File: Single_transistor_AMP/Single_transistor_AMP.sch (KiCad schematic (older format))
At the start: 9 parts, among them J1 Signal_IN, J2 Signal_OUT, Q1 BC337

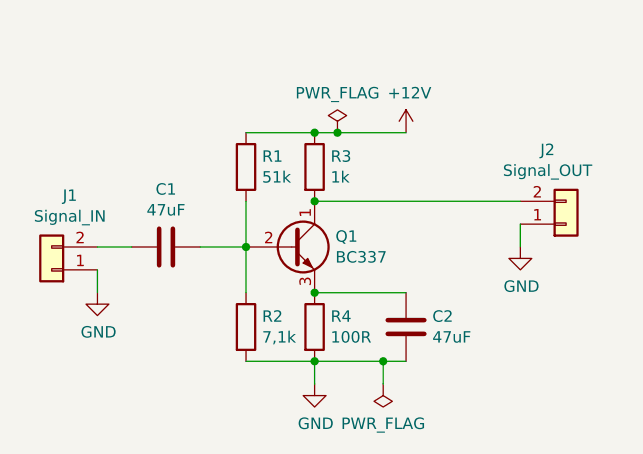
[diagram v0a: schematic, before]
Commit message: Labojums: Pievienots savienotājs +12V barošanai
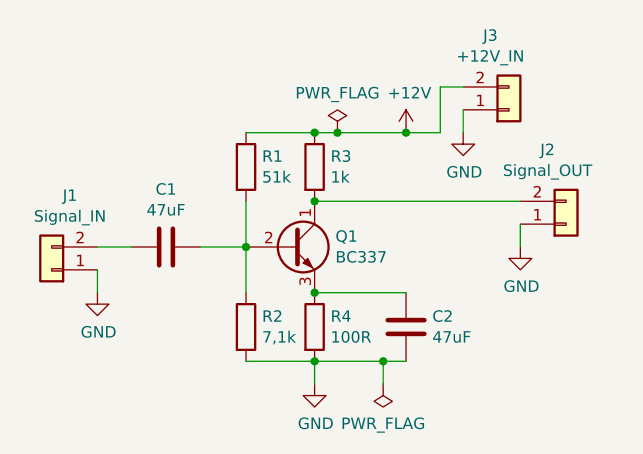
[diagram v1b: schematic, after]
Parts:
- added J3: +12V_IN, symbol Connector_Generic:Conn_01x02
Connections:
- net +12V: now also J3.2 (Pin_2)
- net GND: now also J3.1 (Pin_1)
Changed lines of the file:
@@
 Wire Wire Line
 	5950 4550 6050 4550
+$Comp
+L Connector_Generic:Conn_01x02 J3
+U 1 1 5C9CA615
+P 6500 3450
+F 0 "J3" H 6419 3125 50  0000 C CNN
+F 1 "+12V_IN" H 6419 3216 50  0000 C CNN
+F 2 "" H 6500 3450 50  0001 C CNN
+F 3 "~" H 6500 3450 50  0001 C CNN
+	1    6500 3450
+	1    0    0    1
+$EndComp
+Wire Wire Line
+	6050 3550 6200 3550
+Wire Wire Line
+	6200 3550 6200 3350
+Wire Wire Line
+	6200 3350 6300 3350
+Connection ~ 6050 3550
+Wire Wire Line
+	6300 3450 6300 3550
+$Comp
+L power:GND #PWR05
+U 1 1 5C9CB3FB
+P 6300 3550
+F 0 "#PWR05" H 6300 3300 50  0001 C CNN
+F 1 "GND" H 6305 3377 50  0000 C CNN
+F 2 "" H 6300 3550 50  0001 C CNN
+F 3 "" H 6300 3550 50  0001 C CNN
+	1    6300 3550
+	1    0    0    -1
+$EndComp
 $EndSCHEMATC

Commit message: Izlabots Single_transistor_AMP proj. (datulapas, footprints)
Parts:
- C1, C2: footprint (none) -> Single_transistor_AMP:CAPPRD250W55D630H600
- J1, J2, J3: footprint (none) -> Single_transistor_AMP:SHDR2W90P0X508_1X2_1016X950X1500P_Conn
- Q1: footprint Package_TO_SOT_THT:TO-92_Inline -> Single_transistor_AMP:Pkg_TO_SOT_THT-TO-92_Inline
- R1, R4: footprint (none) -> Single_transistor_AMP:R_2512_6332Metric
- R2: footprint (none) -> Single_transistor_AMP:R_2010_5025Metric
- R3: footprint (none) -> Single_transistor_AMP:R_1218_3246Metric
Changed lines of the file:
@@
 EESchema Schematic File Version 4
 LIBS:Single_transistor_AMP-cache
-EELAYER 29 0
+EELAYER 26 0
 EELAYER END
 $Descr A4 11693 8268
@@
 F 0 "Q1" H 5741 4096 50  0000 L CNN
 F 1 "BC337" H 5741 4005 50  0000 L CNN
-F 2 "Package_TO_SOT_THT:TO-92_Inline" H 5750 3975 50  0001 L CIN
+F 2 "Single_transistor_AMP:Pkg_TO_SOT_THT-TO-92_Inline" H 5750 3975 50  0001 L CIN
 F 3 "https://www.mouser.com/ds/2/302/BC817_BC817W_BC337-188983.pdf" H 5550 4050 50  0001 L CNN
 	1    5550 4050
@@
 F 0 "R2" H 5420 4446 50  0000 L CNN
 F 1 "7,1k" H 5420 4355 50  0000 L CNN
-F 2 "" V 5280 4400 50  0001 C CNN
-F 3 "~" H 5350 4400 50  0001 C CNN
+F 2 "Single_transistor_AMP:R_2010_5025Metric" V 5280 4400 50  0001 C CNN
+F 3 "https://eu.mouser.com/datasheet/2/447/PYu-RC_Group_51_RoHS_L_10-1527934.pdf" H 5350 4400 50  0001 C CNN
 	1    5350 4400
 	1    0    0    -1
@@
 F 0 "R3" H 5720 3746 50  0000 L CNN
 F 1 "1k" H 5720 3655 50  0000 L CNN
-F 2 "" V 5580 3700 50  0001 C CNN
-F 3 "~" H 5650 3700 50  0001 C CNN
+F 2 "Single_transistor_AMP:R_1218_3246Metric" V 5580 3700 50  0001 C CNN
+F 3 "https://eu.mouser.com/datasheet/2/447/yageodocoutput-1290830.pdf" H 5650 3700 50  0001 C CNN
 	1    5650 3700
 	1    0    0    -1
@@
 F 0 "R4" H 5720 4446 50  0000 L CNN
 F 1 "100R" H 5720 4355 50  0000 L CNN
-F 2 "" V 5580 4400 50  0001 C CNN
-F 3 "~" H 5650 4400 50  0001 C CNN
+F 2 "Single_transistor_AMP:R_2512_6332Metric" V 5580 4400 50  0001 C CNN
+F 3 "https://eu.mouser.com/datasheet/2/447/PYu-AC_51_RoHS_L_6-1152827.pdf" H 5650 4400 50  0001 C CNN
 	1    5650 4400
 	1    0    0    -1
@@
 F 0 "C1" V 4748 4050 50  0000 C CNN
 F 1 "47uF" V 4839 4050 50  0000 C CNN
-F 2 "" H 5038 3900 50  0001 C CNN
-F 3 "~" H 5000 4050 50  0001 C CNN
+F 2 "Single_transistor_AMP:CAPPRD250W55D630H600" H 5038 3900 50  0001 C CNN
+F 3 "https://eu.mouser.com/datasheet/2/315/AAB8000C265-1267026.pdf" H 5000 4050 50  0001 C CNN
 	1    5000 4050
 	0    1    1    0
@@
 F 0 "C2" H 5935 4354 50  0000 R CNN
 F 1 "47uF" H 5935 4445 50  0000 R CNN
-F 2 "" H 6088 4250 50  0001 C CNN
-F 3 "~" H 6050 4400 50  0001 C CNN
+F 2 "Single_transistor_AMP:CAPPRD250W55D630H600" H 6088 4250 50  0001 C CNN
+F 3 "https://eu.mouser.com/datasheet/2/315/AAB8000C265-1267026.pdf" H 6050 4400 50  0001 C CNN
 	1    6050 4400
 	-1   0    0    1
@@
 F 0 "J1" H 4420 3825 50  0000 C CNN
 F 1 "Signal_IN" H 4420 3916 50  0000 C CNN
-F 2 "" H 4500 4150 50  0001 C CNN
-F 3 "~" H 4500 4150 50  0001 C CNN
+F 2 "Single_transistor_AMP:SHDR2W90P0X508_1X2_1016X950X1500P_Conn" H 4500 4150 50  0001 C CNN
+F 3 "https://eu.mouser.com/datasheet/2/324/ItemDetail_1888687-919494.pdf" H 4500 4150 50  0001 C CNN
 	1    4500 4150
 	-1   0    0    1
@@
 F 0 "J2" H 6669 3625 50  0000 C CNN
 F 1 "Signal_OUT" H 6669 3716 50  0000 C CNN
-F 2 "" H 6750 3950 50  0001 C CNN
-F 3 "~" H 6750 3950 50  0001 C CNN
+F 2 "Single_transistor_AMP:SHDR2W90P0X508_1X2_1016X950X1500P_Conn" H 6750 3950 50  0001 C CNN
+F 3 "https://eu.mouser.com/datasheet/2/324/ItemDetail_1888687-919494.pdf" H 6750 3950 50  0001 C CNN
 	1    6750 3950
 	1    0    0    1
@@
 F 0 "R1" H 5420 3746 50  0000 L CNN
 F 1 "51k" H 5420 3655 50  0000 L CNN
-F 2 "" V 5280 3700 50  0001 C CNN
-F 3 "~" H 5350 3700 50  0001 C CNN
+F 2 "Single_transistor_AMP:R_2512_6332Metric" V 5280 3700 50  0001 C CNN
+F 3 "https://eu.mouser.com/datasheet/2/447/PYu-AC_51_RoHS_L_6-1152827.pdf" H 5350 3700 50  0001 C CNN
 	1    5350 3700
 	1    0    0    -1
@@
 F 0 "J3" H 6419 3125 50  0000 C CNN
 F 1 "+12V_IN" H 6419 3216 50  0000 C CNN
-F 2 "" H 6500 3450 50  0001 C CNN
-F 3 "~" H 6500 3450 50  0001 C CNN
+F 2 "Single_transistor_AMP:SHDR2W90P0X508_1X2_1016X950X1500P_Conn" H 6500 3450 50  0001 C CNN
+F 3 "https://eu.mouser.com/datasheet/2/324/ItemDetail_1888687-919494.pdf" H 6500 3450 50  0001 C CNN
 	1    6500 3450
 	1    0    0    1

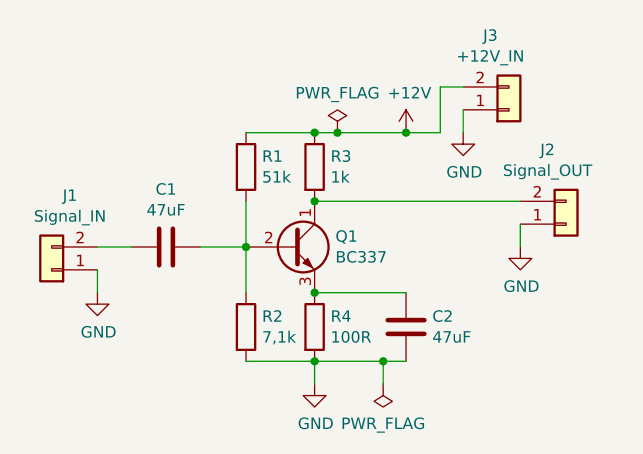
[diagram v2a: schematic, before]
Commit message: Papildināts Single_transistor_AMP projekts, pēc 8.lekcijas m.d. nosacījumiem (darbs ar Pcbnew)
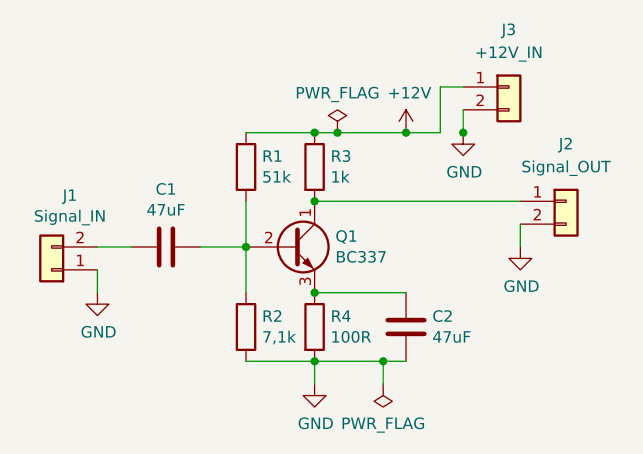
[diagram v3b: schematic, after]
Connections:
- net +12V: now also J3.1 (Pin_1); no longer J3.2 (Pin_2)
- net GND: now also J2.2 (Pin_2), J3.2 (Pin_2); no longer J2.1 (Pin_1), J3.1 (Pin_1)
- net at Q1.1 (C), R3.2: now also J2.1 (Pin_1); no longer J2.2 (Pin_2)
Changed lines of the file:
@@
 EESchema Schematic File Version 4
 LIBS:Single_transistor_AMP-cache
-EELAYER 26 0
+EELAYER 29 0
 EELAYER END
 $Descr A4 11693 8268
@@
 L Connector_Generic:Conn_01x02 J2
 U 1 1 5C8A2EFA
-P 6750 3950
-F 0 "J2" H 6669 3625 50  0000 C CNN
-F 1 "Signal_OUT" H 6669 3716 50  0000 C CNN
-F 2 "Single_transistor_AMP:SHDR2W90P0X508_1X2_1016X950X1500P_Conn" H 6750 3950 50  0001 C CNN
-F 3 "https://eu.mouser.com/datasheet/2/324/ItemDetail_1888687-919494.pdf" H 6750 3950 50  0001 C CNN
-	1    6750 3950
-	1    0    0    1
+P 6750 3850
+F 0 "J2" H 6750 4100 50  0000 C CNN
+F 1 "Signal_OUT" H 6750 4000 50  0000 C CNN
+F 2 "Single_transistor_AMP:SHDR2W90P0X508_1X2_1016X950X1500P_Conn" H 6750 3850 50  0001 C CNN
+F 3 "https://eu.mouser.com/datasheet/2/324/ItemDetail_1888687-919494.pdf" H 6750 3850 50  0001 C CNN
+	1    6750 3850
+	1    0    0    -1
 $EndComp
 $Comp
@@
 Wire Wire Line
 	5650 3850 6550 3850
-Wire Wire Line
-	6550 3950 6550 4050
 Connection ~ 5650 3550
 Wire Wire Line
@@
 L Connector_Generic:Conn_01x02 J3
 U 1 1 5C9CA615
-P 6500 3450
-F 0 "J3" H 6419 3125 50  0000 C CNN
-F 1 "+12V_IN" H 6419 3216 50  0000 C CNN
-F 2 "Single_transistor_AMP:SHDR2W90P0X508_1X2_1016X950X1500P_Conn" H 6500 3450 50  0001 C CNN
-F 3 "https://eu.mouser.com/datasheet/2/324/ItemDetail_1888687-919494.pdf" H 6500 3450 50  0001 C CNN
-	1    6500 3450
-	1    0    0    1
+P 6500 3350
+F 0 "J3" H 6500 3600 50  0000 C CNN
+F 1 "+12V_IN" H 6500 3500 50  0000 C CNN
+F 2 "Single_transistor_AMP:SHDR2W90P0X508_1X2_1016X950X1500P_Conn" H 6500 3350 50  0001 C CNN
+F 3 "https://eu.mouser.com/datasheet/2/324/ItemDetail_1888687-919494.pdf" H 6500 3350 50  0001 C CNN
+	1    6500 3350
+	1    0    0    -1
 $EndComp
 Wire Wire Line
@@
 	1    0    0    -1
 $EndComp
+Wire Wire Line
+	6550 3950 6550 4050
+Connection ~ 6300 3550
 $EndSCHEMATC

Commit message: Pabeigts 9.lekcijā norādītais mājasdarbs
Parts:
- C1: footprint Single_transistor_AMP:CAPPRD250W55D630H600 -> Single_transistor_AMP:CAPC1608X120N
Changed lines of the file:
@@
 F 0 "C1" V 4748 4050 50  0000 C CNN
 F 1 "47uF" V 4839 4050 50  0000 C CNN
-F 2 "Single_transistor_AMP:CAPPRD250W55D630H600" H 5038 3900 50  0001 C CNN
-F 3 "https://eu.mouser.com/datasheet/2/315/AAB8000C265-1267026.pdf" H 5000 4050 50  0001 C CNN
+F 2 "Single_transistor_AMP:CAPC1608X120N" H 5038 3900 50  0001 C CNN
+F 3 "https://eu.mouser.com/datasheet/2/281/ZRB18AR60J476ME01-01-1065054.pdf" H 5000 4050 50  0001 C CNN
 	1    5000 4050
 	0    1    1    0
@@
 Wire Wire Line
 	6550 3950 6550 4050
-Connection ~ 6300 3550
 $EndSCHEMATC
